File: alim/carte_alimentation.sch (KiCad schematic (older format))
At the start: 27 parts, among them J11 Conn_01x02_Male, J12 Conn_01x02_Male, J21 Conn_01x02_Male, J22 Conn_01x02_Male, J31 Conn_01x02_Male, J32 Conn_01x02_Male, J40 Conn_01x02_Male, J41 Conn_01x02_Male, J42 Conn_01x02_Male, J43 Conn_01x02_Male, U1 LM2576T-5, U2 LM2576T-5, U3 LM2576T-5

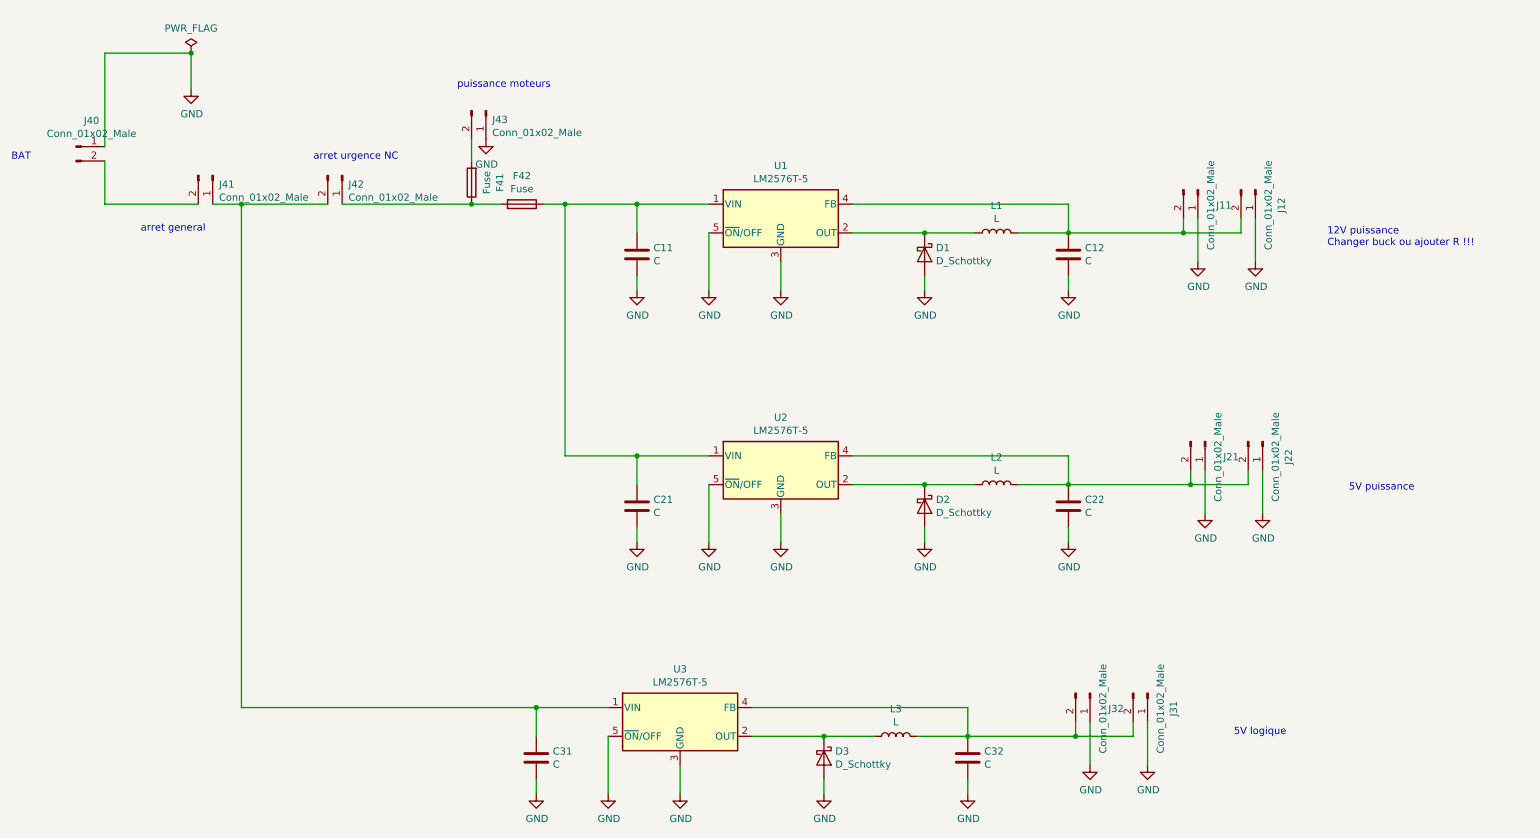
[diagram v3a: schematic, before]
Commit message: ajout empreintes, reste celles du fusibles ajout resitance boucle de retour buck 12v
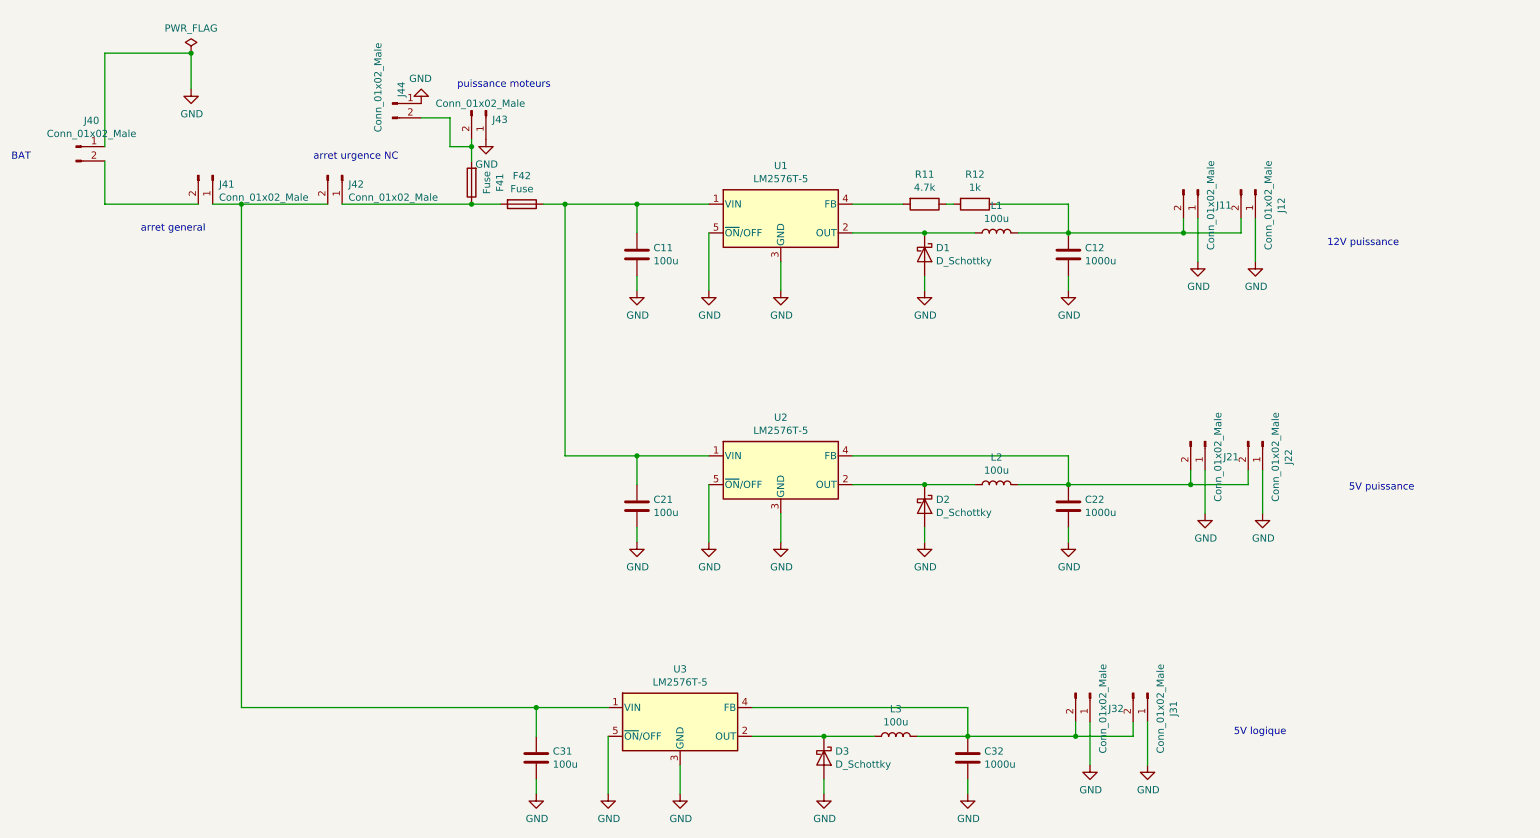
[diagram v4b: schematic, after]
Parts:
- added J44: Conn_01x02_Male, TerminalBlock:TerminalBlock_bornier-2_P5.08mm, symbol Connector:Conn_01x02_Male
- added R11: 4.7k, Resistor_THT:R_Axial_DIN0411_L9.9mm_D3.6mm_P12.70mm_Horizontal, symbol Device:R
- added R12: 1k, Resistor_THT:R_Axial_DIN0411_L9.9mm_D3.6mm_P12.70mm_Horizontal, symbol Device:R
- C11, C21, C31: value C -> 100u
- C12, C22, C32: value C -> 1000u
- L1, L2, L3: value L -> 100u; footprint (none) -> Inductor_THT:L_Toroid_Vertical_L24.6mm_W15.5mm_P11.44mm_Pulse_KM-4
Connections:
- net GND: now also J44.1 (Pin_1)
- net at C12.2, J11.2 (Pin_2), J12.2 (Pin_2)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: now also R12.1; no longer U1.4 (FB)
- net at F41.2, J43.2 (Pin_2): now also J44.2 (Pin_2)
- new net: R11.2, U1.4 (FB)
- new net: R11.1, R12.2
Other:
- note added: "12V puissance"
- note removed: "12V puissance \nChanger buck ou ajouter R !!!\n"
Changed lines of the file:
@@
 P 8200 4100
 F 0 "C22" H 8085 4054 50  0000 R CNN
-F 1 "C" H 8085 4145 50  0000 R CNN
+F 1 "1000u" H 8085 4145 50  0000 R CNN
 F 2 "Capacitor_THT:CP_Radial_D10.0mm_P5.00mm" H 8238 3950 50  0001 C CNN
 F 3 "~" H 8200 4100 50  0001 C CNN
@@
 P 7700 3950
 F 0 "L2" V 7890 3950 50  0000 C CNN
-F 1 "L" V 7799 3950 50  0000 C CNN
-F 2 "" H 7700 3950 50  0001 C CNN
+F 1 "100u" V 7799 3950 50  0000 C CNN
+F 2 "Inductor_THT:L_Toroid_Vertical_L24.6mm_W15.5mm_P11.44mm_Pulse_KM-4" H 7700 3950 50  0001 C CNN
 F 3 "~" H 7700 3950 50  0001 C CNN
 	1    7700 3950
@@
 P 5200 4100
 F 0 "C21" H 5315 4146 50  0000 L CNN
-F 1 "C" H 5315 4055 50  0000 L CNN
+F 1 "100u" H 5315 4055 50  0000 L CNN
 F 2 "Capacitor_THT:CP_Radial_D10.0mm_P5.00mm" H 5238 3950 50  0001 C CNN
 F 3 "~" H 5200 4100 50  0001 C CNN
@@
 P 8200 2350
 F 0 "C12" H 8085 2304 50  0000 R CNN
-F 1 "C" H 8085 2395 50  0000 R CNN
+F 1 "1000u" H 8085 2395 50  0000 R CNN
 F 2 "Capacitor_THT:CP_Radial_D10.0mm_P5.00mm" H 8238 2200 50  0001 C CNN
 F 3 "~" H 8200 2350 50  0001 C CNN
@@
 P 7700 2200
 F 0 "L1" V 7890 2200 50  0000 C CNN
-F 1 "L" V 7799 2200 50  0000 C CNN
-F 2 "" H 7700 2200 50  0001 C CNN
+F 1 "100u" V 7799 2200 50  0000 C CNN
+F 2 "Inductor_THT:L_Toroid_Vertical_L24.6mm_W15.5mm_P11.44mm_Pulse_KM-4" H 7700 2200 50  0001 C CNN
 F 3 "~" H 7700 2200 50  0001 C CNN
 	1    7700 2200
@@
 $EndComp
 Wire Wire Line
-	6700 2000 8200 2000
+	6700 2000 7050 2000
 Wire Wire Line
 	8200 2000 8200 2200
@@
 P 5200 2350
 F 0 "C11" H 5315 2396 50  0000 L CNN
-F 1 "C" H 5315 2305 50  0000 L CNN
+F 1 "100u" H 5315 2305 50  0000 L CNN
 F 2 "Capacitor_THT:CP_Radial_D10.0mm_P5.00mm" H 5238 2200 50  0001 C CNN
 F 3 "~" H 5200 2350 50  0001 C CNN
@@
 P 7500 5850
 F 0 "C32" H 7385 5804 50  0000 R CNN
-F 1 "C" H 7385 5895 50  0000 R CNN
+F 1 "1000u" H 7385 5895 50  0000 R CNN
 F 2 "Capacitor_THT:CP_Radial_D10.0mm_P5.00mm" H 7538 5700 50  0001 C CNN
 F 3 "~" H 7500 5850 50  0001 C CNN
@@
 P 7000 5700
 F 0 "L3" V 7190 5700 50  0000 C CNN
-F 1 "L" V 7099 5700 50  0000 C CNN
-F 2 "" H 7000 5700 50  0001 C CNN
+F 1 "100u" V 7099 5700 50  0000 C CNN
+F 2 "Inductor_THT:L_Toroid_Vertical_L24.6mm_W15.5mm_P11.44mm_Pulse_KM-4" H 7000 5700 50  0001 C CNN
 F 3 "~" H 7000 5700 50  0001 C CNN
 	1    7000 5700
@@
 P 4500 5850
 F 0 "C31" H 4615 5896 50  0000 L CNN
-F 1 "C" H 4615 5805 50  0000 L CNN
+F 1 "100u" H 4615 5805 50  0000 L CNN
 F 2 "Capacitor_THT:CP_Radial_D10.0mm_P5.00mm" H 4538 5700 50  0001 C CNN
 F 3 "~" H 4500 5850 50  0001 C CNN
@@
 5V puissance
 Text Notes 10000 2300 0    50   ~ 0
-12V puissance \nChanger buck ou ajouter R !!!\n
+12V puissance
 Text Notes 850  1700 0    50   ~ 0
 BAT\n
@@
 P 4150 1350
 F 0 "J43" V 4212 1394 50  0000 L CNN
-F 1 "Conn_01x02_Male" V 4303 1394 50  0000 L CNN
+F 1 "Conn_01x02_Male" V 4100 1000 50  0000 L CNN
 F 2 "TerminalBlock:TerminalBlock_bornier-2_P5.08mm" H 4150 1350 50  0001 C CNN
 F 3 "~" H 4150 1350 50  0001 C CNN
@@
 $EndComp
 Wire Wire Line
-	4050 1700 4050 1550
+	4050 1700 4050 1600
 Wire Wire Line
 	3150 2000 4050 2000
@@
 Wire Wire Line
 	4700 2000 5200 2000
+$Comp
+L Device:R R11
+U 1 1 5DEED7D0
+P 7200 2000
+F 0 "R11" V 6993 2000 50  0000 C CNN
+F 1 "4.7k" V 7084 2000 50  0000 C CNN
+F 2 "Resistor_THT:R_Axial_DIN0411_L9.9mm_D3.6mm_P12.70mm_Horizontal" V 7130 2000 50  0001 C CNN
+F 3 "~" H 7200 2000 50  0001 C CNN
+	1    7200 2000
+	0    1    1    0
+$EndComp
+Wire Wire Line
+	7350 2000 7400 2000
+$Comp
+L Device:R R12
+U 1 1 5DEEDB25
+P 7550 2000
+F 0 "R12" V 7343 2000 50  0000 C CNN
+F 1 "1k" V 7434 2000 50  0000 C CNN
+F 2 "Resistor_THT:R_Axial_DIN0411_L9.9mm_D3.6mm_P12.70mm_Horizontal" V 7480 2000 50  0001 C CNN
+F 3 "~" H 7550 2000 50  0001 C CNN
+	1    7550 2000
+	0    1    1    0
+$EndComp
+Wire Wire Line
+	7700 2000 8200 2000
+$Comp
+L Connector:Conn_01x02_Male J44
+U 1 1 5DEFFDEA
+P 3500 1300
+F 0 "J44" V 3562 1344 50  0000 L CNN
+F 1 "Conn_01x02_Male" V 3400 1100 50  0000 L CNN
+F 2 "TerminalBlock:TerminalBlock_bornier-2_P5.08mm" H 3500 1300 50  0001 C CNN
+F 3 "~" H 3500 1300 50  0001 C CNN
+	1    3500 1300
+	1    0    0    -1
+$EndComp
+Wire Wire Line
+	3700 1400 3900 1400
+Wire Wire Line
+	3900 1400 3900 1600
+Wire Wire Line
+	3900 1600 4050 1600
+Connection ~ 4050 1600
+Wire Wire Line
+	4050 1600 4050 1550
+$Comp
+L power:GND #PWR0124
+U 1 1 5DF0F3E5
+P 3700 1300
+F 0 "#PWR0124" H 3700 1050 50  0001 C CNN
+F 1 "GND" H 3705 1127 50  0000 C CNN
+F 2 "" H 3700 1300 50  0001 C CNN
+F 3 "" H 3700 1300 50  0001 C CNN
+	1    3700 1300
+	-1   0    0    1
+$EndComp
 $EndSCHEMATC

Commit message: creation empreinte fusible, tout debut du routage
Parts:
- added HS1, HS2, HS3: Heatsink, symbol Mechanical:Heatsink
- F41, F42: footprint (none) -> fusible:fusible_alim
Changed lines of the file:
@@
 EESchema Schematic File Version 4
-LIBS:carte_alimentation-cache
 EELAYER 30 0
 EELAYER END
@@
 F 0 "F41" V 3853 1850 50  0000 C CNN
 F 1 "Fuse" V 3944 1850 50  0000 C CNN
-F 2 "" V 3980 1850 50  0001 C CNN
+F 2 "fusible:fusible_alim" V 3980 1850 50  0001 C CNN
 F 3 "~" H 4050 1850 50  0001 C CNN
 	1    4050 1850
@@
 F 0 "F42" V 4203 2000 50  0000 C CNN
 F 1 "Fuse" V 4294 2000 50  0000 C CNN
-F 2 "" V 4330 2000 50  0001 C CNN
+F 2 "fusible:fusible_alim" V 4330 2000 50  0001 C CNN
 F 3 "~" H 4400 2000 50  0001 C CNN
 	1    4400 2000
@@
 	-1   0    0    1
 $EndComp
+$Comp
+L Mechanical:Heatsink HS1
+U 1 1 5DF31D2D
+P 6200 1600
+F 0 "HS1" H 6342 1721 50  0000 L CNN
+F 1 "Heatsink" H 6342 1630 50  0000 L CNN
+F 2 "" H 6212 1600 50  0001 C CNN
+F 3 "~" H 6212 1600 50  0001 C CNN
+	1    6200 1600
+	1    0    0    -1
+$EndComp
+$Comp
+L Mechanical:Heatsink HS2
+U 1 1 5DF33999
+P 6150 3400
+F 0 "HS2" H 6292 3521 50  0000 L CNN
+F 1 "Heatsink" H 6292 3430 50  0000 L CNN
+F 2 "" H 6162 3400 50  0001 C CNN
+F 3 "~" H 6162 3400 50  0001 C CNN
+	1    6150 3400
+	1    0    0    -1
+$EndComp
+$Comp
+L Mechanical:Heatsink HS3
+U 1 1 5DF33D93
+P 5700 5150
+F 0 "HS3" H 5842 5271 50  0000 L CNN
+F 1 "Heatsink" H 5842 5180 50  0000 L CNN
+F 2 "" H 5712 5150 50  0001 C CNN
+F 3 "~" H 5712 5150 50  0001 C CNN
+	1    5700 5150
+	1    0    0    -1
+$EndComp
 $EndSCHEMATC

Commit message: retrait radiateur (pas besoin cf robot 2A), debut routage
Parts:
- removed HS1, HS2, HS3: Heatsink, symbol Mechanical:Heatsink
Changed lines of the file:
@@
 encoding utf-8
 Sheet 1 1
-Title ""
-Date ""
-Rev ""
-Comp ""
+Title "Carte Alim"
+Date "dec 2019"
+Rev "v1"
+Comp "EirBoat"
 Comment1 ""
 Comment2 ""
@@
 	-1   0    0    1
 $EndComp
-$Comp
-L Mechanical:Heatsink HS1
-U 1 1 5DF31D2D
-P 6200 1600
-F 0 "HS1" H 6342 1721 50  0000 L CNN
-F 1 "Heatsink" H 6342 1630 50  0000 L CNN
-F 2 "" H 6212 1600 50  0001 C CNN
-F 3 "~" H 6212 1600 50  0001 C CNN
-	1    6200 1600
-	1    0    0    -1
-$EndComp
-$Comp
-L Mechanical:Heatsink HS2
-U 1 1 5DF33999
-P 6150 3400
-F 0 "HS2" H 6292 3521 50  0000 L CNN
-F 1 "Heatsink" H 6292 3430 50  0000 L CNN
-F 2 "" H 6162 3400 50  0001 C CNN
-F 3 "~" H 6162 3400 50  0001 C CNN
-	1    6150 3400
-	1    0    0    -1
-$EndComp
-$Comp
-L Mechanical:Heatsink HS3
-U 1 1 5DF33D93
-P 5700 5150
-F 0 "HS3" H 5842 5271 50  0000 L CNN
-F 1 "Heatsink" H 5842 5180 50  0000 L CNN
-F 2 "" H 5712 5150 50  0001 C CNN
-F 3 "~" H 5712 5150 50  0001 C CNN
-	1    5700 5150
-	1    0    0    -1
-$EndComp
 $EndSCHEMATC

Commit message: correction polarisation condensateur, ajout texte, compactage verif rapide boucle de courant
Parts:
- removed C12, C22, C32: 1000u, Capacitor_THT:CP_Radial_D10.0mm_P5.00mm, symbol Device:C
- added C12, C22, C32: 1000u, Capacitor_THT:CP_Radial_D10.0mm_P5.00mm, symbol Device:CP
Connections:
- net GND: now also C12.2, C22.2, C32.2
- net at J21.2 (Pin_2), J22.2 (Pin_2), L2.2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: now also C22.1
- net at J11.2 (Pin_2), J12.2 (Pin_2), L1.2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: now also C12.1
- net at J31.2 (Pin_2), J32.2 (Pin_2), L3.2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: now also C32.1
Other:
- note added: "Hack feedback\n5.74 KOhms"
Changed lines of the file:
@@
-$EndComp
-$Comp
-L Device:C C22
-U 1 1 5DE01F50
-P 8200 4100
-F 0 "C22" H 8085 4054 50  0000 R CNN
-F 1 "1000u" H 8085 4145 50  0000 R CNN
-F 2 "Capacitor_THT:CP_Radial_D10.0mm_P5.00mm" H 8238 3950 50  0001 C CNN
-F 3 "~" H 8200 4100 50  0001 C CNN
-	1    8200 4100
-	-1   0    0    1
 $EndComp
 $Comp
@@
 	7200 3950 6700 3950
 Wire Wire Line
-	7850 3950 8200 3950
+	7850 3950 8000 3950
 $Comp
 L power:GND #PWR0101
@@
 	1    6200 2100
 	1    0    0    -1
-$EndComp
-$Comp
-L Device:C C12
-U 1 1 5DE2299D
-P 8200 2350
-F 0 "C12" H 8085 2304 50  0000 R CNN
-F 1 "1000u" H 8085 2395 50  0000 R CNN
-F 2 "Capacitor_THT:CP_Radial_D10.0mm_P5.00mm" H 8238 2200 50  0001 C CNN
-F 3 "~" H 8200 2350 50  0001 C CNN
-	1    8200 2350
-	-1   0    0    1
 $EndComp
 $Comp
@@
 $EndComp
 $Comp
-L Device:C C32
-U 1 1 5DE2627B
-P 7500 5850
-F 0 "C32" H 7385 5804 50  0000 R CNN
-F 1 "1000u" H 7385 5895 50  0000 R CNN
-F 2 "Capacitor_THT:CP_Radial_D10.0mm_P5.00mm" H 7538 5700 50  0001 C CNN
-F 3 "~" H 7500 5850 50  0001 C CNN
-	1    7500 5850
-	-1   0    0    1
-$EndComp
-$Comp
 L Device:L L3
 U 1 1 5DE26281
@@
 	-1   0    0    1
 $EndComp
+Text Notes 7150 1650 0    50   ~ 0
+Hack feedback\n5.74 KOhms
+$Comp
+L Device:CP C22
+U 1 1 5DF78C22
+P 8200 4100
+F 0 "C22" H 8318 4146 50  0000 L CNN
+F 1 "1000u" H 8318 4055 50  0000 L CNN
+F 2 "Capacitor_THT:CP_Radial_D10.0mm_P5.00mm" H 8238 3950 50  0001 C CNN
+F 3 "~" H 8200 4100 50  0001 C CNN
+	1    8200 4100
+	1    0    0    -1
+$EndComp
+Wire Wire Line
+	8000 3950 8200 3950
+$Comp
+L Device:CP C12
+U 1 1 5DF7D5A2
+P 8200 2350
+F 0 "C12" H 8318 2396 50  0000 L CNN
+F 1 "1000u" H 8318 2305 50  0000 L CNN
+F 2 "Capacitor_THT:CP_Radial_D10.0mm_P5.00mm" H 8238 2200 50  0001 C CNN
+F 3 "~" H 8200 2350 50  0001 C CNN
+	1    8200 2350
+	1    0    0    -1
+$EndComp
+$Comp
+L Device:CP C32
+U 1 1 5DF817D2
+P 7500 5850
+F 0 "C32" H 7618 5896 50  0000 L CNN
+F 1 "1000u" H 7618 5805 50  0000 L CNN
+F 2 "Capacitor_THT:CP_Radial_D10.0mm_P5.00mm" H 7538 5700 50  0001 C CNN
+F 3 "~" H 7500 5850 50  0001 C CNN
+	1    7500 5850
+	1    0    0    -1
+$EndComp
 $EndSCHEMATC

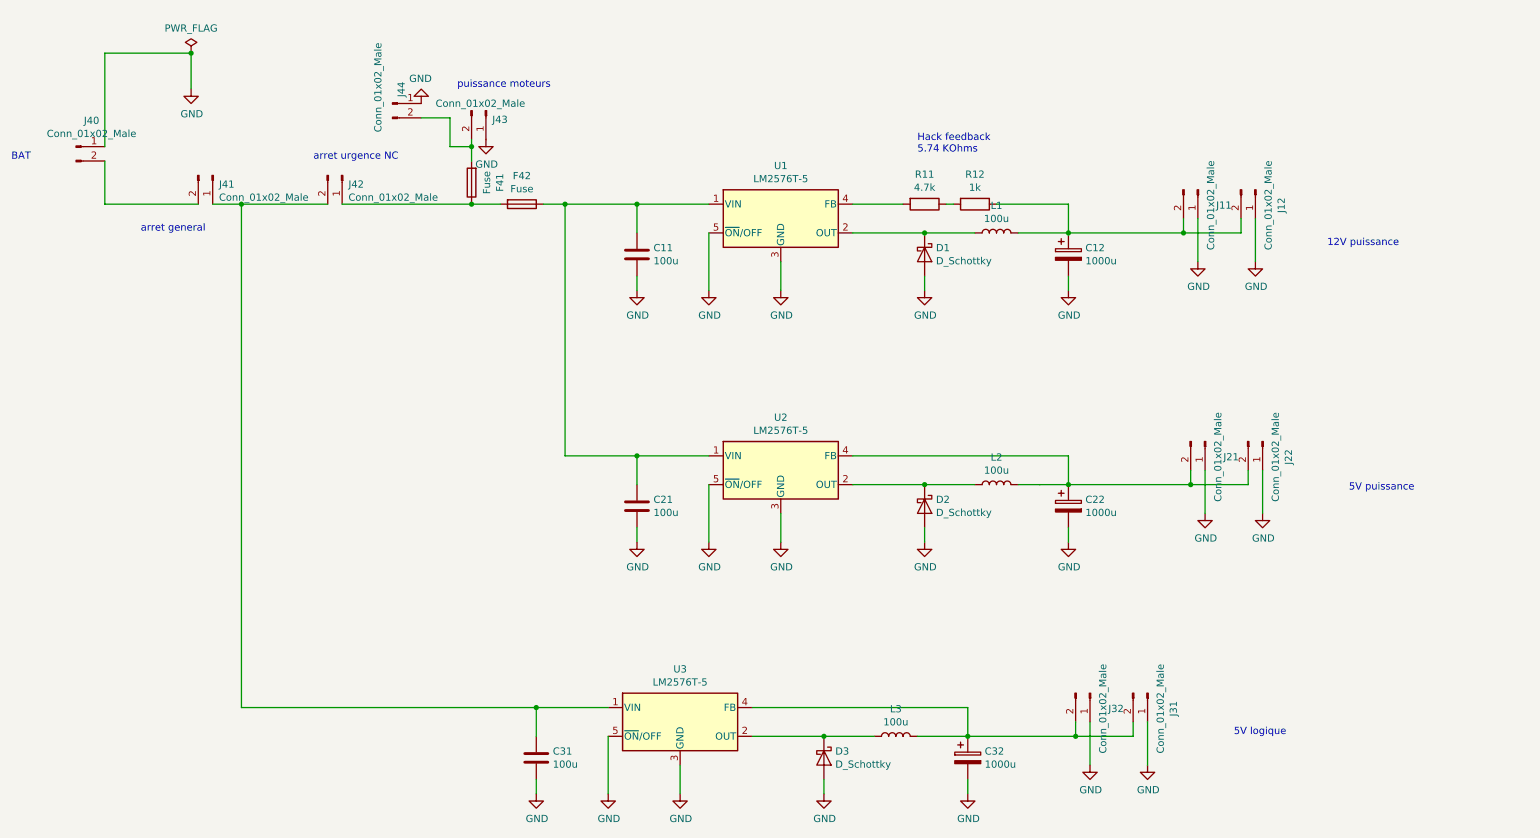
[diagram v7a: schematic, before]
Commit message: retrait arret general, il sera entre la batterie et la carte de secu
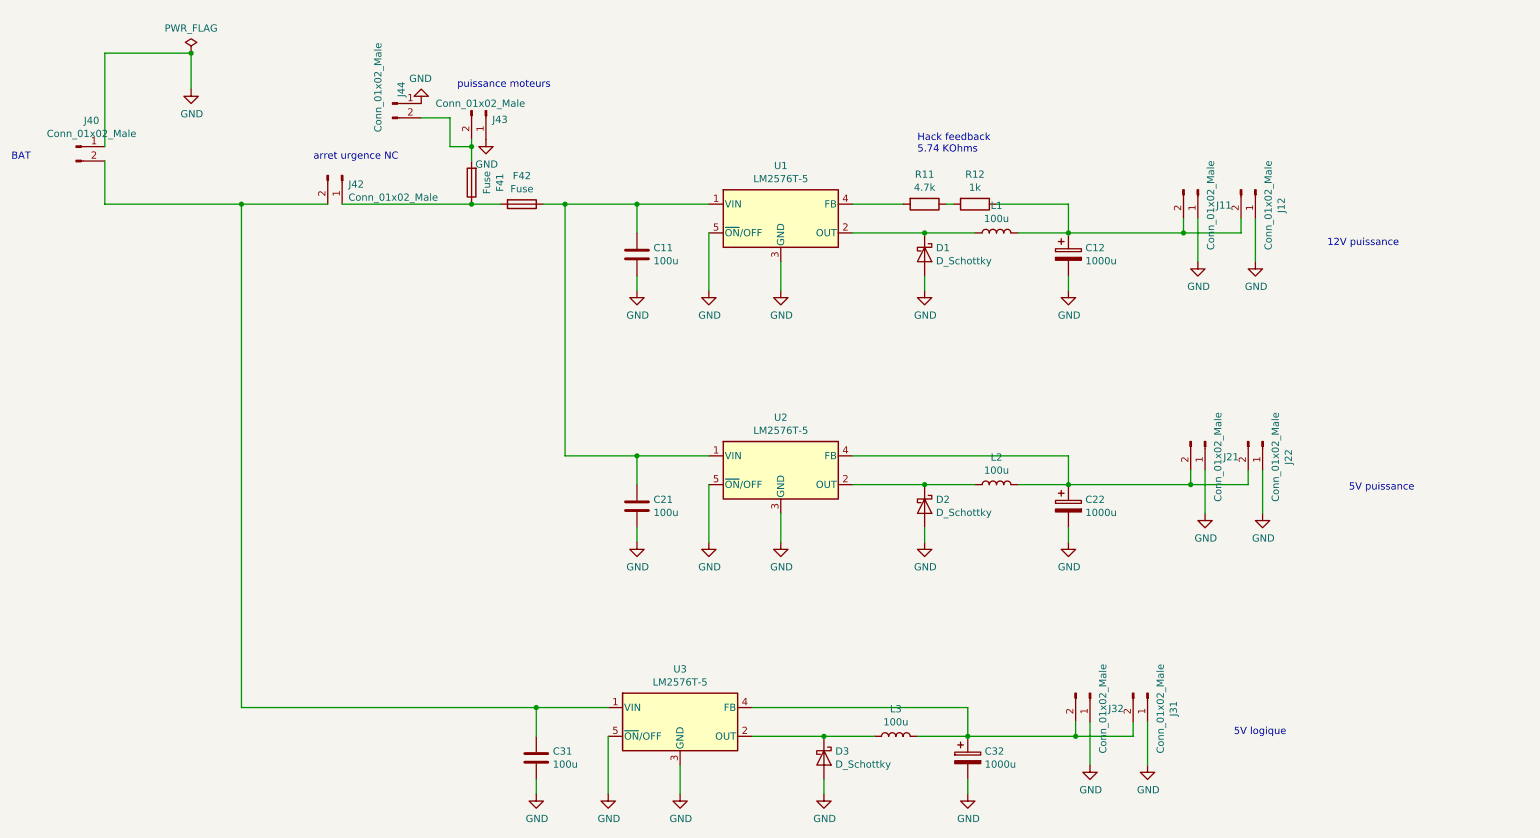
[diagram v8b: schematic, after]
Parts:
- removed J41: Conn_01x02_Male, TerminalBlock:TerminalBlock_bornier-2_P5.08mm, symbol Connector:Conn_01x02_Male
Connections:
- net at J40.2 (Pin_2): now also C31.1, J42.2 (Pin_2), U3.1 (VIN)
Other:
- note removed: "arret general"
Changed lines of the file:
@@
 Wire Wire Line
 	7200 3950 6700 3950
-Wire Wire Line
-	7850 3950 8000 3950
 $Comp
 L power:GND #PWR0101
@@
 Wire Wire Line
 	1500 950  1500 1600
-Text Notes 1750 2200 0    50   ~ 0
-arret general
 $Comp
 L power:PWR_FLAG #FLG0101
@@
 	0    1    1    0
 $EndComp
-$Comp
-L Connector:Conn_01x02_Male J41
-U 1 1 5DE5159F
-P 2250 1800
-F 0 "J41" V 2312 1844 50  0000 L CNN
-F 1 "Conn_01x02_Male" V 2403 1844 50  0000 L CNN
-F 2 "TerminalBlock:TerminalBlock_bornier-2_P5.08mm" H 2250 1800 50  0001 C CNN
-F 3 "~" H 2250 1800 50  0001 C CNN
-	1    2250 1800
-	0    1    1    0
-$EndComp
-Wire Wire Line
-	2250 2000 2450 2000
 Connection ~ 2450 2000
 Text Notes 3950 1200 0    50   ~ 0
@@
 Wire Wire Line
 	3150 2000 4050 2000
-Wire Wire Line
-	1500 2000 2150 2000
 Connection ~ 4050 2000
 Wire Wire Line
@@
 	1    0    0    -1
 $EndComp
-Wire Wire Line
-	8000 3950 8200 3950
 $Comp
 L Device:CP C12
@@
 	1    0    0    -1
 $EndComp
+Wire Wire Line
+	7850 3950 8200 3950
+Wire Wire Line
+	1500 2000 2450 2000
 $EndSCHEMATC
